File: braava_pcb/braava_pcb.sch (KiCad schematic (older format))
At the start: 6 parts, among them J1 Conn_01x18, J2 Conn_01x18

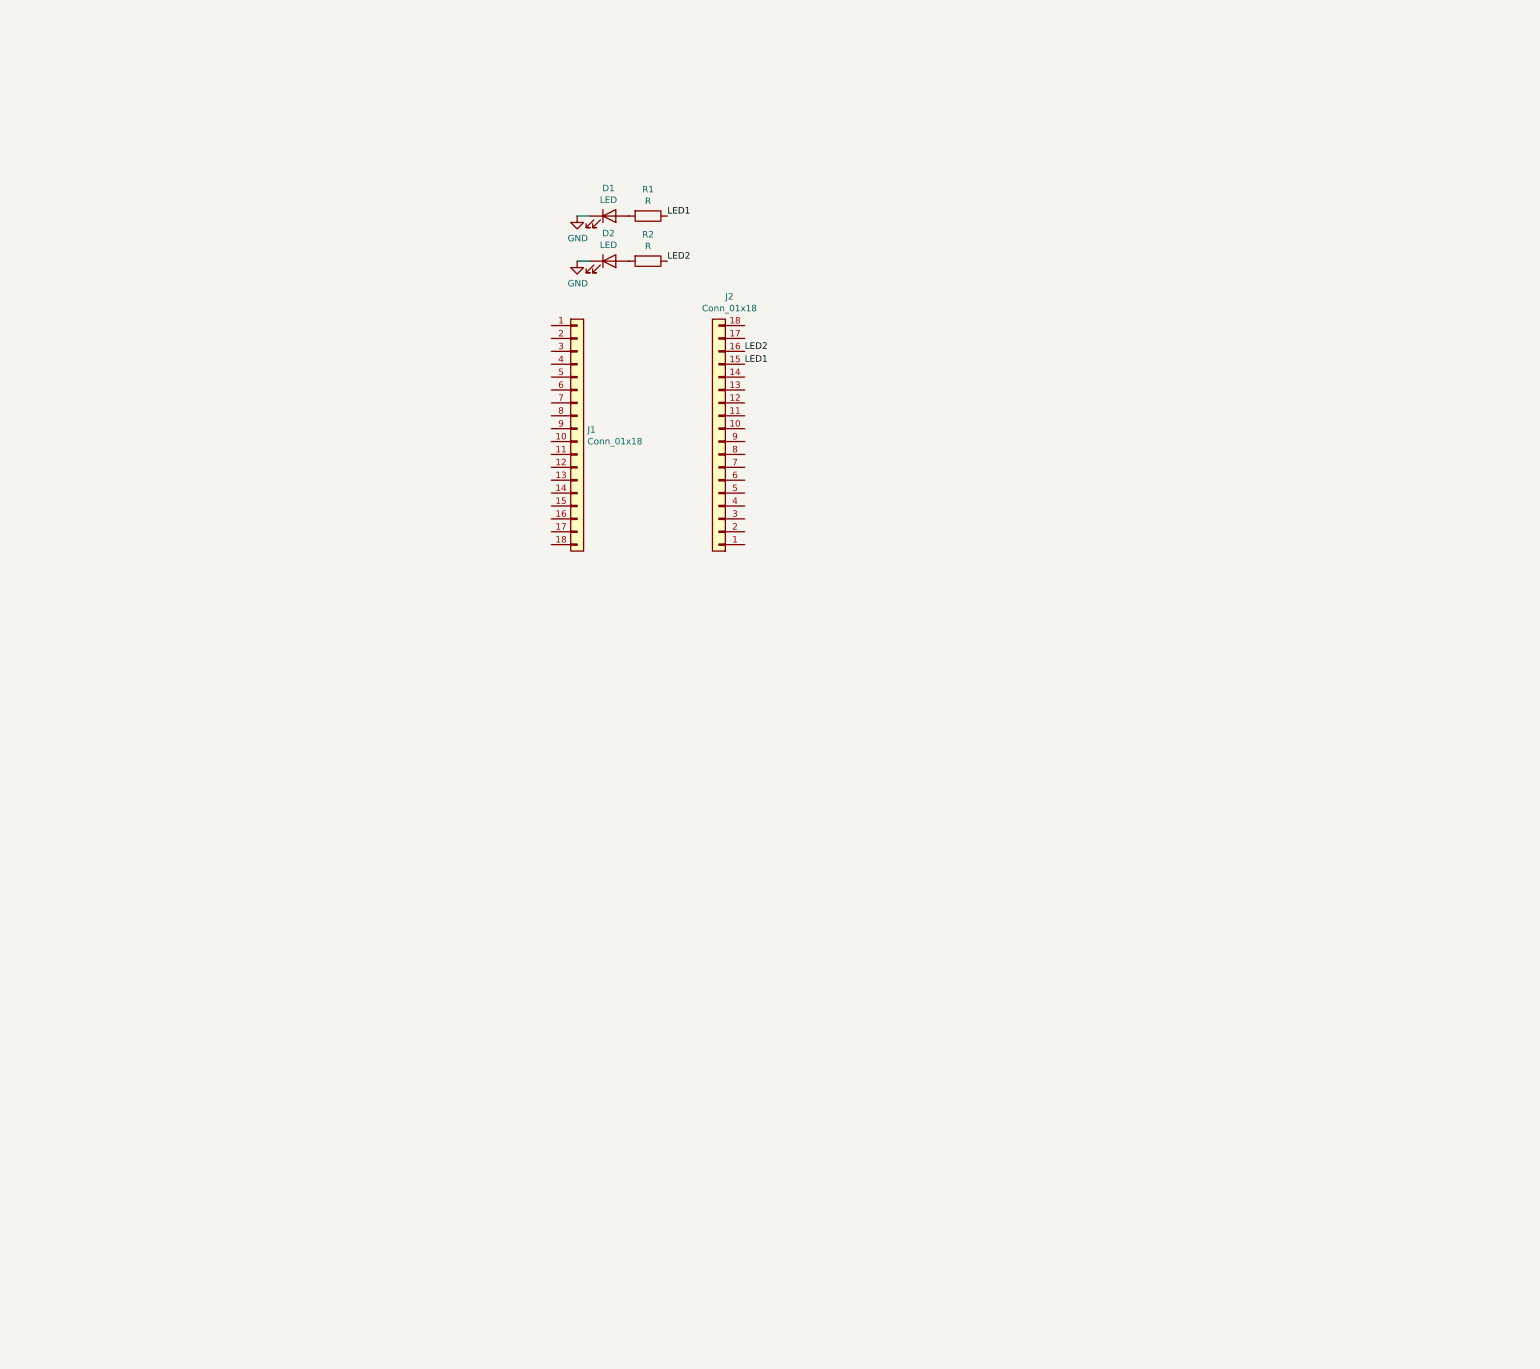
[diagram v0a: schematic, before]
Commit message: Most components added to schematic
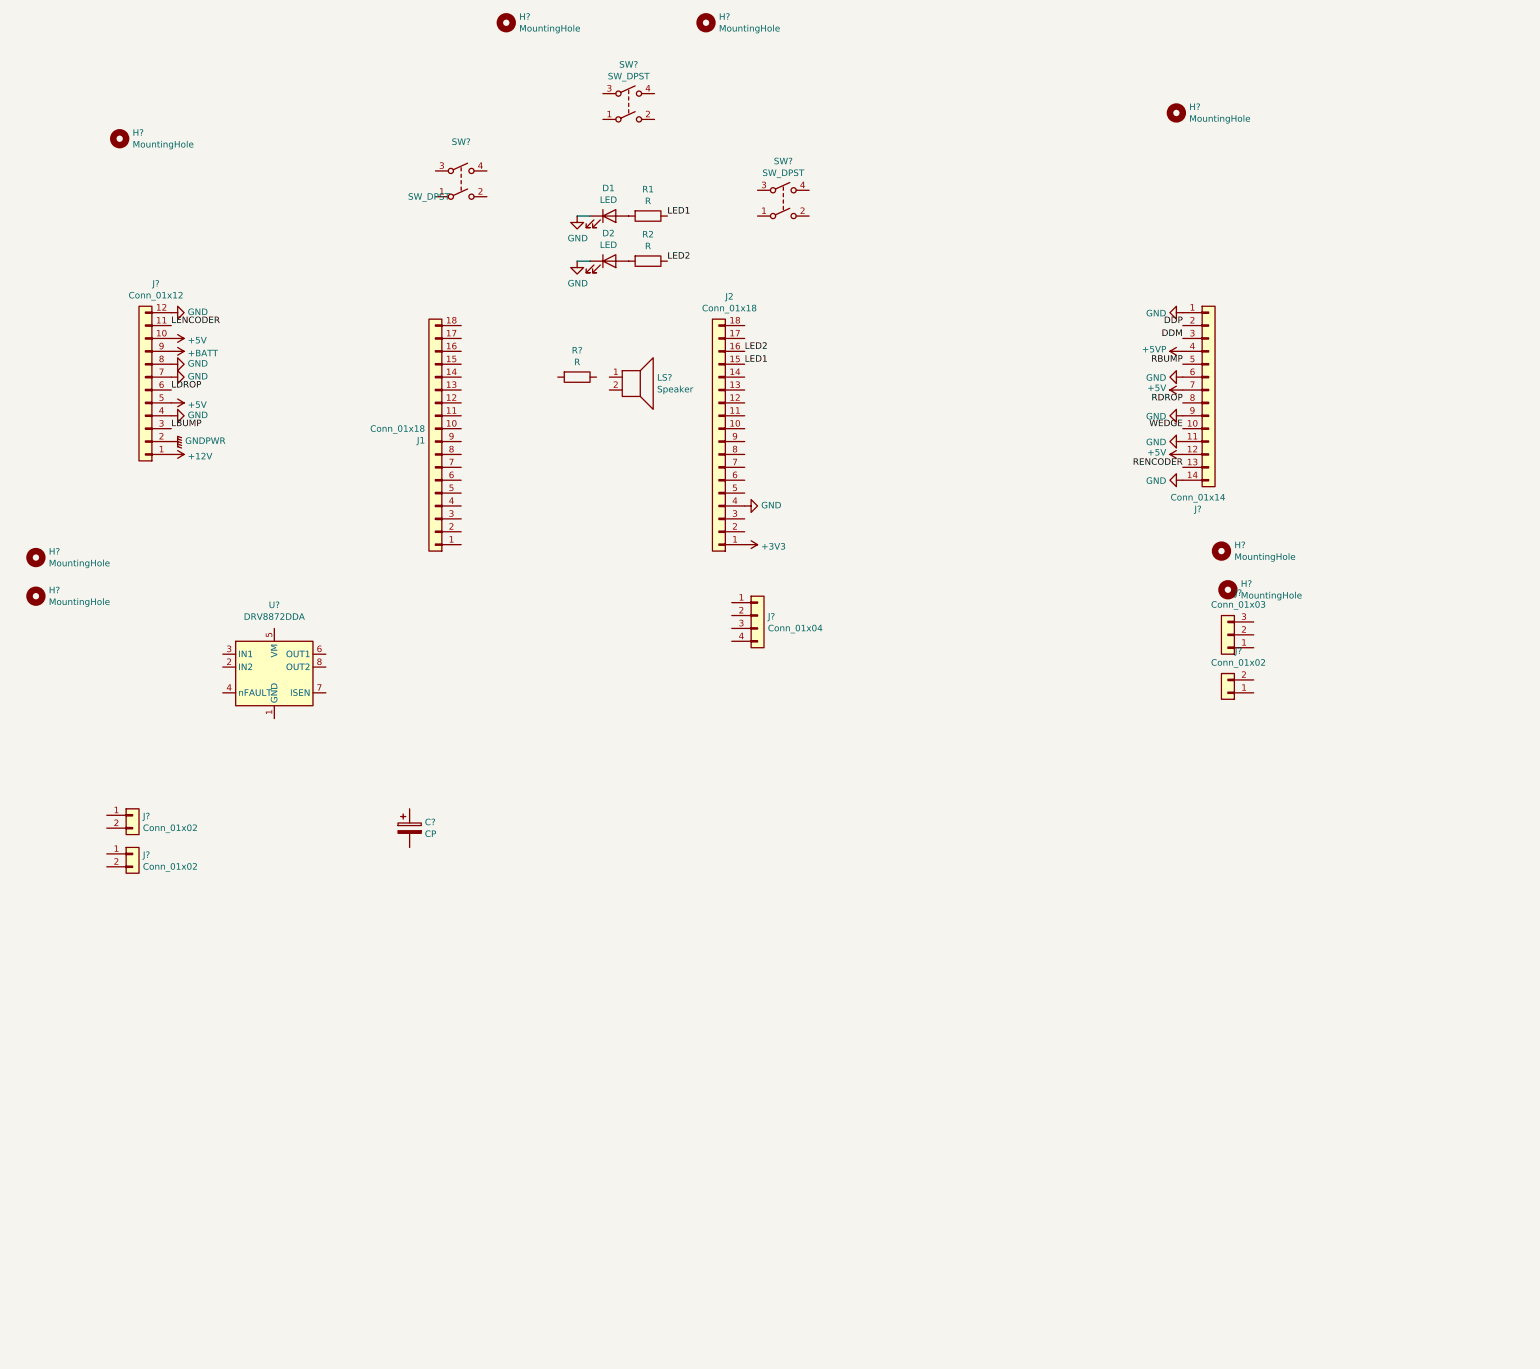
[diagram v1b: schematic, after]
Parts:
- added C?: CP, symbol Device:CP
- added H? (x8): MountingHole, symbol Mechanical:MountingHole
- added J?: Conn_01x03, symbol Connector_Generic:Conn_01x03
- added J? (x3): Conn_01x02, symbol Connector_Generic:Conn_01x02
- added J?: Conn_01x12, symbol Connector_Generic:Conn_01x12
- added J?: Conn_01x14, symbol Connector_Generic:Conn_01x14
- added J?: Conn_01x04, symbol Connector_Generic:Conn_01x04
- added LS?: Speaker, symbol Device:Speaker
- added R?: R, Resistor_SMD:R_0603_1608Metric, symbol Device:R
- added SW? (x3): SW_DPST, symbol Switch:SW_DPST
- added U?: DRV8872DDA, Package_SO:Texas_HTSOP-8-1EP_3.9x4.9mm_P1.27mm_EP2.95x4.9mm_Mask2.4x3.1mm_ThermalVias, symbol Driver_Motor:DRV8872DDA
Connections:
- net GND: now also J2.4 (Pin_4), J?.1 (Pin_1), J?.11 (Pin_11), J?.12 (Pin_12), J?.14 (Pin_14), J?.4 (Pin_4), J?.6 (Pin_6), J?.7 (Pin_7), J?.8 (Pin_8), J?.9 (Pin_9)
- net +3V3: now reaches J2.1 (Pin_1)
- new net: U?.1 (GND), U?.9 (GND)
- new net +12V: J?.1 (Pin_1)
- new net +5V: J?.10 (Pin_10), J?.12 (Pin_12), J?.5 (Pin_5), J?.7 (Pin_7)
- new net +5VP: J?.4 (Pin_4)
- new net +BATT: J?.9 (Pin_9)
- new net DDM: J?.3 (Pin_3)
- new net DDP: J?.2 (Pin_2)
- new net GNDPWR: J?.2 (Pin_2)
- new net LBUMP: J?.3 (Pin_3)
- new net LDROP: J?.6 (Pin_6)
- new net LENCODER: J?.11 (Pin_11)
- new net RBUMP: J?.5 (Pin_5)
- new net RDROP: J?.8 (Pin_8)
- new net RENCODER: J?.13 (Pin_13)
- new net WEDGE: J?.10 (Pin_10)
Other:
- moved on the sheet: J1

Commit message: Motors, switches near completed
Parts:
- removed J?: Conn_01x02, symbol Connector_Generic:Conn_01x02
- removed SW? (x2): SW_DPST, symbol Switch:SW_DPST
- added C? (x4): 47uF, symbol Device:C
- added C? (x4): 0.1uF, symbol Device:C
- added C? (x3): 1uF, symbol Device:C
- added J?: LMOT_Conn_01x02, symbol Connector_Generic:Conn_01x02
- added R? (x3): 4.7K, Resistor_SMD:R_0603_1608Metric, symbol Device:R
- added SW?: SW2_WET, symbol Switch:SW_DPST
- added SW?: SW3_DRY, symbol Switch:SW_DPST
- added U? (x7): DRV8872DDA, Package_SO:Texas_HTSOP-8-1EP_3.9x4.9mm_P1.27mm_EP2.95x4.9mm_Mask2.4x3.1mm_ThermalVias, symbol Driver_Motor:DRV8872DDA
- J?: value Conn_01x03 -> BAT_Conn_01x03
- J?: value Conn_01x02 -> RMOT_Conn_01x02
- J?: value Conn_01x04 -> STEP_Conn_01x04
- SW?: value SW_DPST -> SW1_PWR
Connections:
- net +12V: now also U?.5 (VM), C?.2, C?.2, C?.2, C?.2, C?.2, C?.2, C?.2, C?.2, U?.5 (VM), U?.5 (VM), U?.5 (VM), U?.5 (VM), U?.5 (VM), U?.5 (VM), U?.5 (VM)
- net +3V3: now also R?.1, R?.1, R?.1
- net GND: now also SW?.2, SW?.4, U?.1 (GND), U?.7 (ISEN), U?.9 (GND), C?.1, C?.1, C?.1, C?.1, C?.1, C?.1, C?.1, C?.1, C?.1, C?.1, C?.1, SW?.2, SW?.2, SW?.4, SW?.4, U?.1 (GND), U?.1 (GND), U?.1 (GND), U?.1 (GND), U?.1 (GND), U?.1 (GND), U?.1 (GND), U?.7 (ISEN), U?.7 (ISEN), U?.7 (ISEN), U?.7 (ISEN), U?.7 (ISEN), U?.7 (ISEN), U?.7 (ISEN), U?.9 (GND), U?.9 (GND), U?.9 (GND), U?.9 (GND), U?.9 (GND), U?.9 (GND), U?.9 (GND)
- net LBUMP: now also J1.14 (Pin_14)
- net LDROP: now also J1.13 (Pin_13)
- net LENCODER: now also J1.4 (Pin_4)
- net RBUMP: now also J2.11 (Pin_11)
- net RDROP: now also J2.10 (Pin_10)
- net RENCODER: now also J1.3 (Pin_3)
- net WEDGE: now also J2.9 (Pin_9)
- net A0_PWM1: now reaches J1.1 (Pin_1)
- net A0_PWM1: now also U?.3 (IN1), U?.3 (IN1)
- net SW3_DRY: now reaches J1.10 (Pin_10)
- net SW3_DRY: now also C?.2, R?.2, SW?.1, SW?.3
- net SDA: now reaches J1.11 (Pin_11)
- net SCL: now reaches J1.12 (Pin_12)
- net A1_PWM2: now reaches J1.2 (Pin_2)
- net A1_PWM2: now also U?.2 (IN2), U?.2 (IN2)
- net SW1_PWR: now reaches J1.8 (Pin_8)
- net SW1_PWR: now also SW?.1, SW?.3, C?.2, R?.2
- net SW2_WET: now reaches J1.9 (Pin_9)
- net SW2_WET: now also C?.2, R?.2, SW?.1, SW?.3
- net D6_PWM2: now reaches J2.12 (Pin_12)
- net D6_PWM2: now also U?.2 (IN2), U?.2 (IN2)
- net D5_PWM1: now reaches J2.13 (Pin_13)
- net D5_PWM1: now also U?.3 (IN1), U?.3 (IN1)
- net ESP_TX: now reaches J2.17 (Pin_17)
- net ESP_TX: now also J?.3 (Pin_3)
- net ESP_RX: now reaches J2.18 (Pin_18)
- net ESP_RX: now also J?.2 (Pin_2)
- net IO11_STEP1: now reaches J2.5 (Pin_5)
- net IO11_STEP1: now also U?.2 (IN2), U?.2 (IN2)
- net IO8_STEP1: now reaches J2.6 (Pin_6)
- net IO8_STEP1: now also U?.3 (IN1), U?.3 (IN1)
- net IO7_STEP1: now reaches J2.7 (Pin_7)
- net IO7_STEP1: now also U?.2 (IN2), U?.2 (IN2)
- net IO6_STEP1: now reaches J2.8 (Pin_8)
- net IO6_STEP1: now also U?.3 (IN1), U?.3 (IN1)
- net at J?.1 (Pin_1): now also U?.6 (OUT1), U?.6 (OUT1) (x2)
- net at J?.2 (Pin_2): now also U?.8 (OUT2), U?.8 (OUT2) (x2)
- net at J?.3 (Pin_3): now also U?.6 (OUT1), U?.6 (OUT1)
- net at J?.4 (Pin_4): now also U?.8 (OUT2), U?.8 (OUT2)
- net at U?.4 (nFAULT): now also U?.4 (nFAULT)
- new net: U?.4 (nFAULT), U?.4 (nFAULT) (x3)
- new net: J?.1 (Pin_1), U?.6 (OUT1), U?.6 (OUT1)
- new net: J?.2 (Pin_2), U?.8 (OUT2), U?.8 (OUT2)
- no-connect marks 0 -> 5
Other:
- note added: "BDC motors and STEP motor"
- note added: "Mounting holes"
- note added: "Switches and LEDs"
- moved on the sheet: C?, D1, D2, H?, J1, J?, LS?, R1, R2, R?, SW?, U?
